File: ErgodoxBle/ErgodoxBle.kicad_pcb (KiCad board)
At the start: 2 copper layers, 181.7 x 158.1 mm, 85 parts, among them K0 KEYSW, K1 KEYSW, K10 KEYSW, K11 KEYSW, K12 KEYSW, K13 KEYSW, K14 KEYSW, K15 KEYSW, K16 KEYSW, K2 KEYSW, K20 KEYSW, K21 KEYSW, K22 KEYSW, K23 KEYSW, K24 KEYSW, K25 KEYSW, K26 KEYSW, K3 KEYSW, K30 KEYSW, K31 KEYSW, K32 KEYSW, K33 KEYSW, K34 KEYSW, K35 KEYSW, K36 KEYSW, K4 KEYSW, K40 KEYSW, K41 KEYSW, K42 KEYSW, K43 KEYSW, K44 KEYSW, K45 KEYSW, K46 KEYSW, K5 KEYSW, K54 KEYSW, K55 KEYSW, K56 KEYSW, K6 KEYSW, SW1 SW_PUSH, SW2 SW_PUSH

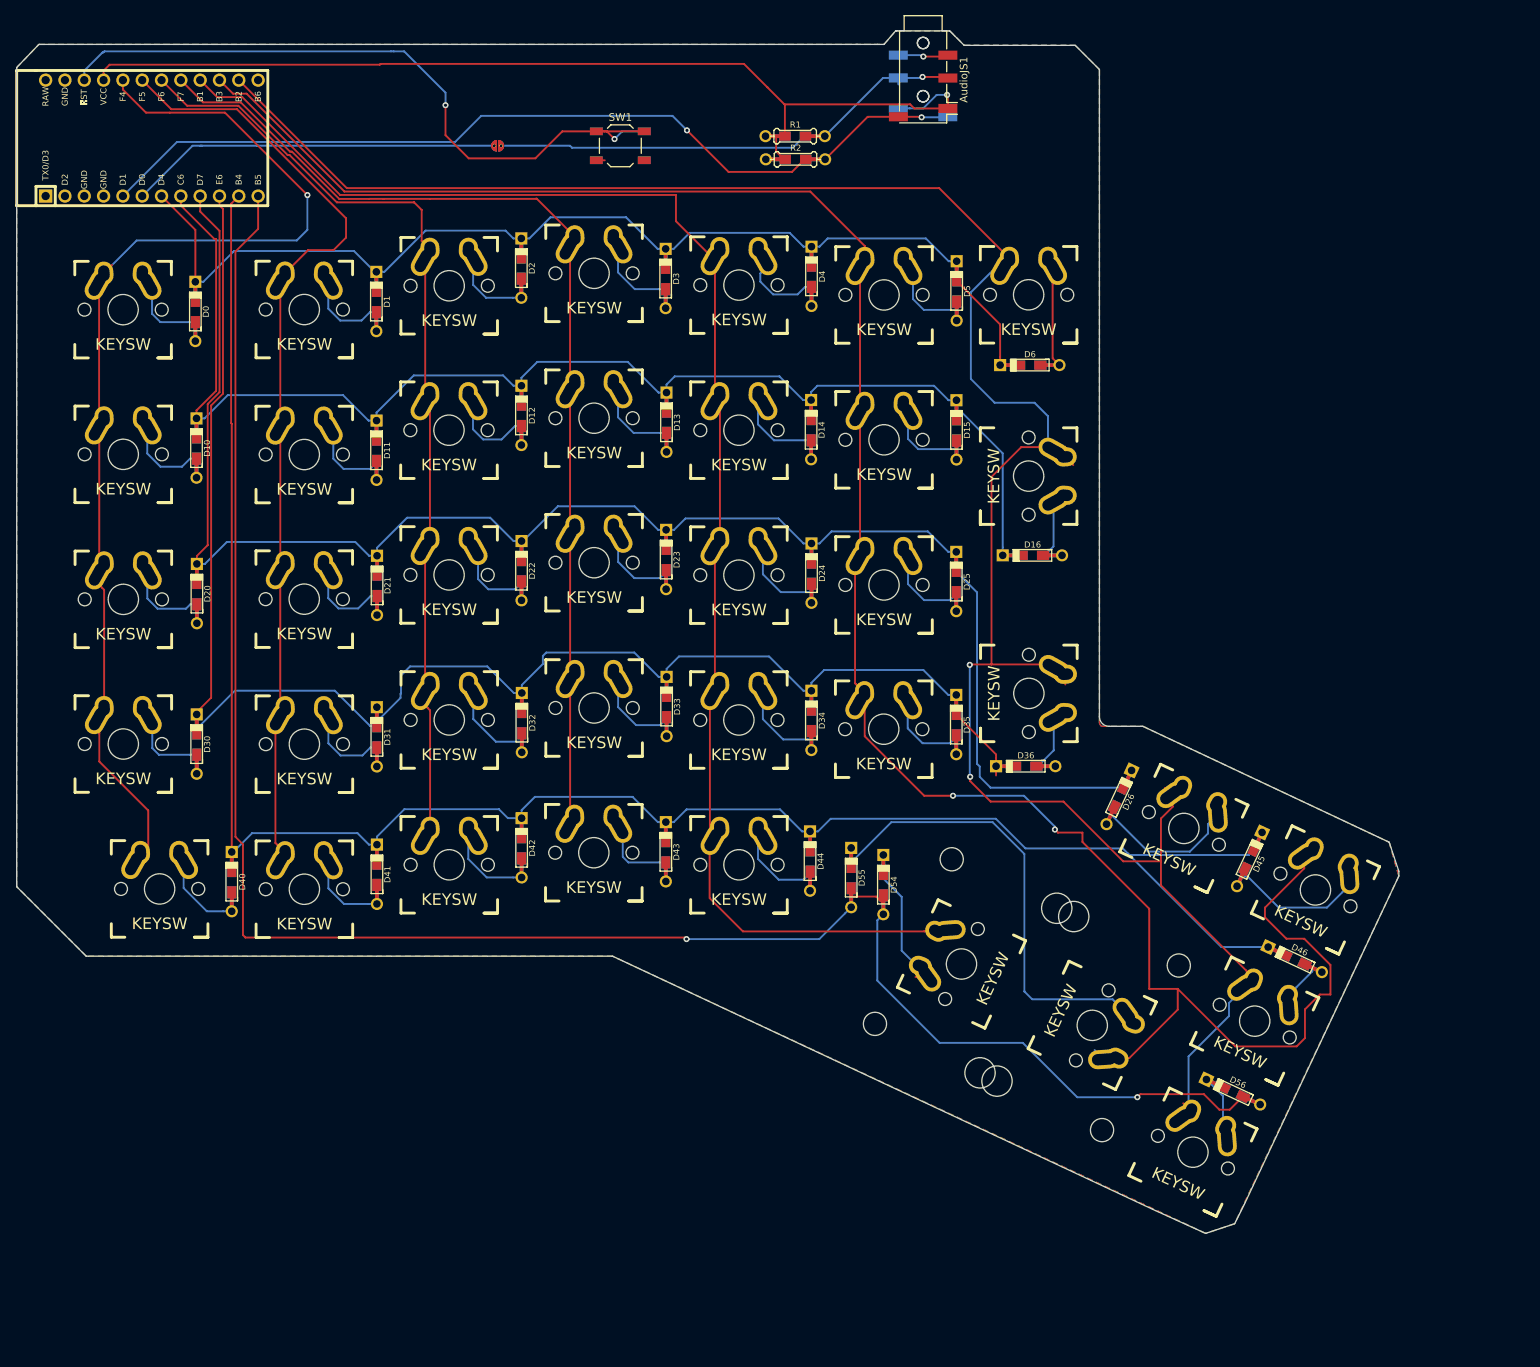
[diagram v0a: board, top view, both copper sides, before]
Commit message: Redo the existing ergodox pcb
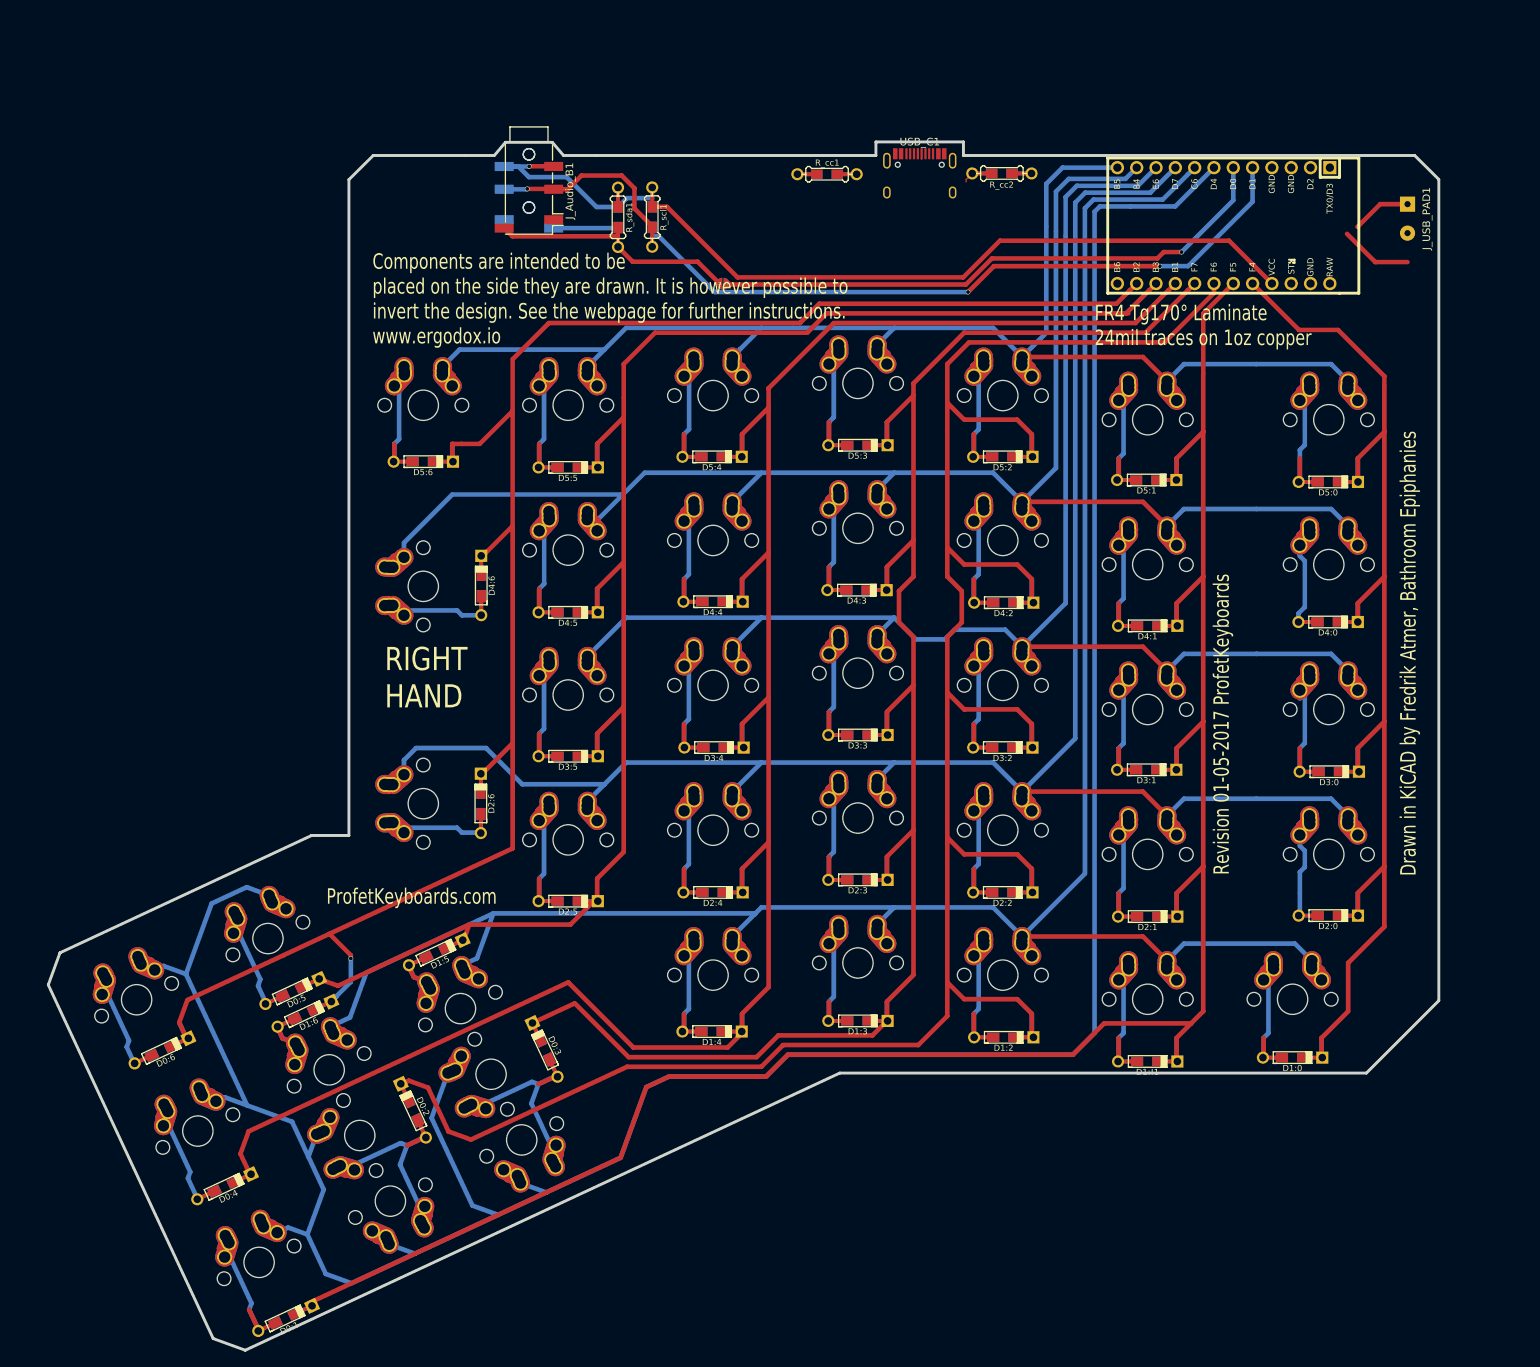
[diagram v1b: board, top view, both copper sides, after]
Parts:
- removed AudioJM1, AudioJS1: AudioJack4, Connector_Audio:Jack_3.5mm_PJ320D_Horizontal
- removed D0, D1, D10, D11, D12, D13, D14, D15, D16, D2, D20, D21, D22, D23, D24, D25, D26, D3, D30, D31, D32, D33, D34, D35, D36, D4, D40, D41, D42, D43, D44, D45, D46, D5, D6: D, Keebio-Parts:Diode-dual
- removed D54, D55, D56: DIODE, Keebio-Parts:Diode-dual
- removed K0, K1, K10, K11, K12, K13, K14, K15, K16, K2, K20, K21, K22, K23, K24, K25, K26, K3, K30, K31, K32, K33, K34, K35, K36, K4, K40, K41, K42, K43, K44, K45, K46, K5, K56, K6: KEYSW, footprints:Mx_Alps_100-dualside
- removed K54, K55: KEYSW, footprints:Mx_Alps_200-dualside
- removed MCU1: ProMicro, Keebio-Parts:ArduinoProMicro
- removed R1, R2: 4.7k, Keebio-Parts:Resistor-Hybrid
- removed SJ1, SJ2: SOLDER_JUMPER, Keebio-Parts:solder_jumper
- removed SW1, SW2: SW_PUSH, Button_Switch_SMD:SW_SPST_TL3342
- added D0:1: D, Keebio-Parts:Diode-dual, F.Cu at (54.2, 185.2)
- added D0:2: D, Keebio-Parts:Diode-dual, F.Cu at (71.1, 157.9)
- added D0:3: D, Keebio-Parts:Diode-dual, F.Cu at (88.4, 149.9)
- added D0:4: D, Keebio-Parts:Diode-dual, F.Cu at (46.2, 167.9)
- added D0:5: D, Keebio-Parts:Diode-dual, F.Cu at (55.2, 142.2)
- added D0:6: D, Keebio-Parts:Diode-dual, F.Cu at (38.0, 150.0)
- added D1:!1: D, Keebio-Parts:Diode-dual, F.Cu at (167.6, 151.4)
- added D1:0: D, Keebio-Parts:Diode-dual, F.Cu at (186.7, 150.9)
- added D1:2: D, Keebio-Parts:Diode-dual, F.Cu at (148.7, 148.2)
- added D1:3: D, Keebio-Parts:Diode-dual, F.Cu at (129.5, 146.1)
- added D1:4: D, Keebio-Parts:Diode-dual, F.Cu at (110.4, 147.4)
- added D1:5: D, Keebio-Parts:Diode-dual, F.Cu at (74.0, 137.1)
- added D1:6: D, Keebio-Parts:Diode-dual, F.Cu at (56.8, 145.2)
- added D2:0: D, Keebio-Parts:Diode-dual, F.Cu at (191.4, 132.2)
- added D2:1: D, Keebio-Parts:Diode-dual, F.Cu at (167.6, 132.3)
- added D2:2: D, Keebio-Parts:Diode-dual, F.Cu at (148.6, 129.2)
- added D2:3: D, Keebio-Parts:Diode-dual, F.Cu at (129.5, 127.5)
- added D2:4: D, Keebio-Parts:Diode-dual, F.Cu at (110.5, 129.2)
- added D2:5: D, Keebio-Parts:Diode-dual, F.Cu at (91.4, 130.3)
- added D2:6: D, Keebio-Parts:Diode-dual, F.Cu at (80.0, 117.4)
- added D3:0: D, Keebio-Parts:Diode-dual, F.Cu at (191.5, 113.3)
- added D3:1: D, Keebio-Parts:Diode-dual, F.Cu at (167.5, 113.0)
- added D3:2: D, Keebio-Parts:Diode-dual, F.Cu at (148.6, 110.1)
- added D3:3: D, Keebio-Parts:Diode-dual, F.Cu at (129.5, 108.5)
- added D3:4: D, Keebio-Parts:Diode-dual, F.Cu at (110.6, 110.1)
- added D3:5: D, Keebio-Parts:Diode-dual, F.Cu at (91.4, 111.3)
- added D4:0: D, Keebio-Parts:Diode-dual, F.Cu at (191.4, 93.6)
- added D4:1: D, Keebio-Parts:Diode-dual, F.Cu at (167.6, 94.1)
- added D4:2: D, Keebio-Parts:Diode-dual, F.Cu at (148.7, 91.1)
- added D4:3: D, Keebio-Parts:Diode-dual, F.Cu at (129.4, 89.4)
- added D4:4: D, Keebio-Parts:Diode-dual, F.Cu at (110.5, 90.9)
- added D4:5: D, Keebio-Parts:Diode-dual, F.Cu at (91.4, 92.3)
- added D4:6: D, Keebio-Parts:Diode-dual, F.Cu at (80.0, 88.8)
- added D5:0: D, Keebio-Parts:Diode-dual, F.Cu at (191.4, 75.2)
- added D5:1: D, Keebio-Parts:Diode-dual, F.Cu at (167.5, 74.9)
- added D5:2: D, Keebio-Parts:Diode-dual, F.Cu at (148.6, 71.9)
- added D5:3: D, Keebio-Parts:Diode-dual, F.Cu at (129.5, 70.4)
- added D5:4: D, Keebio-Parts:Diode-dual, F.Cu at (110.4, 71.9)
- added D5:5: D, Keebio-Parts:Diode-dual, F.Cu at (91.4, 73.3)
- added D5:6: D, Keebio-Parts:Diode-dual, F.Cu at (72.4, 72.5)
- added JP1: SolderJumper_2_Open, Keebio-Parts:solder_jumper, F.Cu at (111.8, 49.1)
- added J_Audio_B1: AudioJack4, Connector_Audio:Jack_3.5mm_PJ320D_Horizontal, F.Cu at (86.3, 36.9)
- added J_Audio_F1: AudioJack4, Connector_Audio:Jack_3.5mm_PJ320D_Horizontal, B.Cu at (86.3, 36.9)
- added J_USB_PAD1: Conn_01x02_Female, Connector_Wire:SolderWirePad_1x02_P3.81mm_Drill0.8mm, F.Cu at (201.8, 38.7)
- added R_cc1: 5.1K, Keebio-Parts:Resistor-Hybrid, F.Cu at (125.5, 34.7)
- added R_cc2: 5.1K, Keebio-Parts:Resistor-Hybrid, F.Cu at (148.5, 34.6)
- added R_scl1: 47k, Keebio-Parts:Resistor-Hybrid, F.Cu at (102.5, 40.4)
- added R_sda1: 47k, Keebio-Parts:Resistor-Hybrid, F.Cu at (98.0, 40.4)
- added SW0:10: SW0:3, Keebio-Parts:Hybrid_PCB_100H_Dual_hole, F.Cu at (81.3, 153.1)
- added SW0:11: SW0:2, Keebio-Parts:Hybrid_PCB_100H_Dual_hole, F.Cu at (64.0, 161.1)
- added SW0:12: SW0:1, Keebio-Parts:Hybrid_PCB_100H_Dual_hole, F.Cu at (50.8, 177.8)
- added SW0:7: SW0:6, Keebio-Parts:Hybrid_PCB_100H_Dual_hole, F.Cu at (34.7, 143.3)
- added SW0:8: SW0:5, Keebio-Parts:Hybrid_PCB_100H_Dual_hole, F.Cu at (52.0, 135.2)
- added SW0:9: SW0:4, Keebio-Parts:Hybrid_PCB_100H_Dual_hole, F.Cu at (42.7, 160.5)
- added SW1:10: SW1:3, Keebio-Parts:Hybrid_PCB_100H_Dual_hole, F.Cu at (129.5, 138.4)
- added SW1:11: SW1:2, Keebio-Parts:Hybrid_PCB_100H_Dual_hole, F.Cu at (148.6, 140.0)
- added SW1:12: SW1:1, Keebio-Parts:Hybrid_PCB_100H_Dual_hole, F.Cu at (167.6, 143.2)
- added SW1:13: SW1:0, Keebio-Parts:Hybrid_PCB_100H_Dual_hole, F.Cu at (186.7, 143.2)
- added SW1:9: SW1:4, Keebio-Parts:Hybrid_PCB_100H_Dual_hole, F.Cu at (110.5, 140.0)
- added SW2:10: SW2:3, Keebio-Parts:Hybrid_PCB_100H_Dual_hole, F.Cu at (129.5, 119.4)
- added SW2:11: SW2:2, Keebio-Parts:Hybrid_PCB_100H_Dual_hole, F.Cu at (148.6, 121.0)
- added SW2:12: SW2:1, Keebio-Parts:Hybrid_PCB_100H_Dual_hole, F.Cu at (167.6, 124.2)
- added SW2:13: SW2:0, Keebio-Parts:Hybrid_PCB_100H_Dual_hole, F.Cu at (191.5, 124.2)
- added SW2:7: SW2:6, Keebio-Parts:Hybrid_PCB_100H_Dual_hole, F.Cu at (72.4, 117.5)
- added SW2:8: SW2:5, Keebio-Parts:Hybrid_PCB_100H_Dual_hole, F.Cu at (91.4, 122.2)
- added SW2:9: SW2:4, Keebio-Parts:Hybrid_PCB_100H_Dual_hole, F.Cu at (110.5, 121.0)
- added SW3:10: SW3:3, Keebio-Parts:Hybrid_PCB_100H_Dual_hole, F.Cu at (129.5, 100.3)
- added SW3:11: SW3:2, Keebio-Parts:Hybrid_PCB_100H_Dual_hole, F.Cu at (148.6, 101.9)
- added SW3:12: SW3:1, Keebio-Parts:Hybrid_PCB_100H_Dual_hole, F.Cu at (167.6, 105.1)
- added SW3:13: SW3:0, Keebio-Parts:Hybrid_PCB_100H_Dual_hole, F.Cu at (191.5, 105.1)
- added SW3:8: SW3:5, Keebio-Parts:Hybrid_PCB_100H_Dual_hole, F.Cu at (91.4, 103.2)
- added SW3:9: SW3:4, Keebio-Parts:Hybrid_PCB_100H_Dual_hole, F.Cu at (110.5, 101.9)
- added SW4:10: SW4:3, Keebio-Parts:Hybrid_PCB_100H_Dual_hole, F.Cu at (129.5, 81.3)
- added SW4:11: SW4:2, Keebio-Parts:Hybrid_PCB_100H_Dual_hole, F.Cu at (148.6, 82.9)
- added SW4:12: SW4:1, Keebio-Parts:Hybrid_PCB_100H_Dual_hole, F.Cu at (167.6, 86.1)
- added SW4:13: SW4:0, Keebio-Parts:Hybrid_PCB_100H_Dual_hole, F.Cu at (191.5, 86.1)
- added SW4:7: SW4:6, Keebio-Parts:Hybrid_PCB_100H_Dual_hole, F.Cu at (72.4, 88.9)
- added SW4:8: SW4:5, Keebio-Parts:Hybrid_PCB_100H_Dual_hole, F.Cu at (91.4, 84.1)
- added SW4:9: SW4:4, Keebio-Parts:Hybrid_PCB_100H_Dual_hole, F.Cu at (110.5, 82.9)
- added SW5:10: SW5:3, Keebio-Parts:Hybrid_PCB_100H_Dual_hole, F.Cu at (129.5, 62.2)
- added SW5:11: SW5:2, Keebio-Parts:Hybrid_PCB_100H_Dual_hole, F.Cu at (148.6, 63.8)
- added SW5:12: SW5:1, Keebio-Parts:Hybrid_PCB_100H_Dual_hole, F.Cu at (167.6, 67.0)
- added SW5:13: SW5:0, Keebio-Parts:Hybrid_PCB_100H_Dual_hole, F.Cu at (191.5, 67.0)
- added SW5:7: SW5:6, Keebio-Parts:Hybrid_PCB_100H_Dual_hole, F.Cu at (72.4, 65.1)
- added SW5:8: SW5:5, Keebio-Parts:Hybrid_PCB_100H_Dual_hole, F.Cu at (91.4, 65.1)
- added SW5:9: SW5:4, Keebio-Parts:Hybrid_PCB_100H_Dual_hole, F.Cu at (110.5, 63.8)
- added SX0:10: SX0:3, Keebio-Parts:Hybrid_PCB_100H_Dual_hole, F.Cu at (85.3, 161.7)
- added SX0:11: SX0:2, Keebio-Parts:Hybrid_PCB_100H_Dual_hole, F.Cu at (68.1, 169.7)
- added SX1:7: SX1:6, Keebio-Parts:Hybrid_PCB_100H_Dual_hole, F.Cu at (60.0, 152.5)
- added SX1:8: SX1:5, Keebio-Parts:Hybrid_PCB_100H_Dual_hole, F.Cu at (77.3, 144.4)
- added USB_C1: HRO-TYPE-C-31-M-12, usbc_footprint:HRO-TYPE-C-31-M-12, F.Cu at (137.7, 39.7)
- added proMicro1: ProMicro, Keebio-Parts:ArduinoProMicro, F.Cu at (177.6, 41.5)
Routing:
- net /ROW0: track 0.00 -> 400.6 mm
- net /ROW1: track 0.00 -> 314.9 mm
- net /COL11: track 0.00 -> 298.0 mm
- net COL6: track 295.5 -> 0.00 mm, vias 2 -> 0
- net /ROW2: track 0.00 -> 284.6 mm
- net COL5: track 283.8 -> 0.00 mm, vias 2 -> 0
- net /COL1: track 0.00 -> 277.3 mm
- net /COL4: track 0.00 -> 267.3 mm
- net ROW4: track 258.6 -> 0.00 mm
- net ROW5: track 250.6 -> 0.00 mm, vias 2 -> 0
- net /ROW4: track 0.00 -> 246.3 mm
- net /COL6: track 0.00 -> 244.2 mm, vias 0 -> 1
- net /ROW3: track 0.00 -> 228.3 mm
- net /COL10: track 0.00 -> 224.1 mm
- net /COL5: track 0.00 -> 219.1 mm
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- removed copper zone on B.Cu, net GND
- removed copper zone on F.Cu, net GND
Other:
- board size 181.7 x 158.1 mm -> 182.8 x 158.9 mm
- net class Default: clearance 0.2 -> 0.3048; trace_width 0.25 -> 0.6; via_dia 0.8 -> 0.6096; via_drill 0.4 -> 0.508
- rule pad_to_mask_clearance: 0.051 -> 0.2032
- rule trace_clearance: 0.2 -> 0.3048
- rule trace_min: 0.2 -> 0.0254
- rule via_min_drill: 0.3 -> 0.2032
- rule via_min_size: 0.4 -> 0.4064
- board text added: "Components are intended to be placed on the side they are drawn. It is however possible to invert the design. See the webpage for further instructions. www.ergodox.io"
- board text added: "Design by Dominic Beauchamp, based on the Key64 by Nestor A. Diaz"
- board text added: "Drawn in KiCAD by Fredrik Atmer, Bathroom Epiphanies"
- board text added: "ErgoDox"
- board text added: "FR4 Tg170° Laminate 24mil traces on 1oz copper"
- board text added: "LEFT HAND"
- board text added: "ProfetKeyboards.com"
- board text added: "RIGHT HAND"
- board text added: "Revision 01-05-2017 ProfetKeyboards"

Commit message: Added USB-C
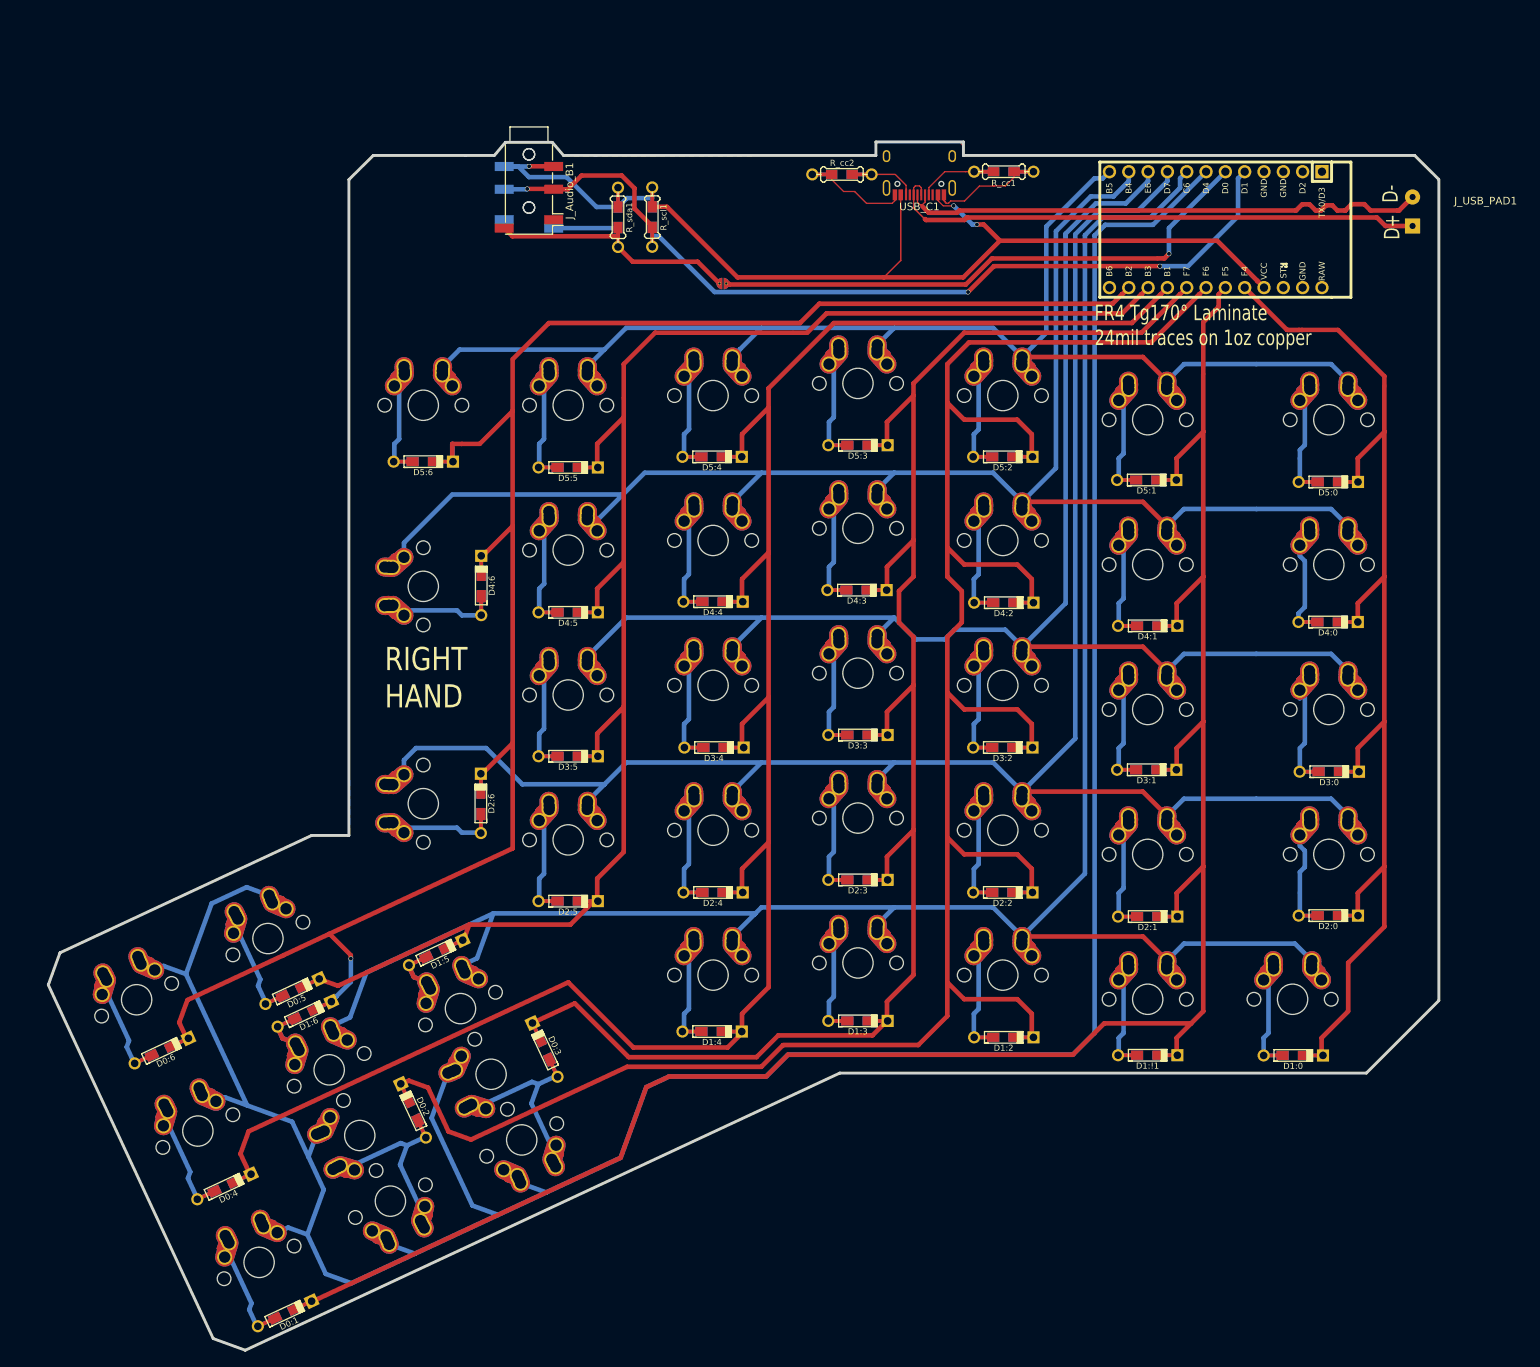
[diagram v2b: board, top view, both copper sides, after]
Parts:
- moved R_cc1 23.2 mm to (148.7, 34.4), turned to 0 degrees
- moved R_cc2 21.0 mm to (127.4, 34.7), turned to 180 degrees
- moved USB_C1 9.98 mm to (137.6, 29.7), turned to 180 degrees
- moved J_USB_PAD1 2.95 mm to (202.5, 41.5), turned to 90 degrees
- moved proMicro1 1.17 mm to (176.6, 42.0)
- moved D1:!1 0.82 mm to (167.6, 150.6)
- moved D0:1 0.62 mm to (54.2, 184.5)
- moved D1:0 0.30 mm to (186.8, 150.6)
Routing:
- net /D+: track 7.84 -> 71.7 mm
- net /D-: track 9.51 -> 71.0 mm
- net GND: track 0.00 -> 23.5 mm
- net /Vcc: track 118.3 -> 140.4 mm, vias 1 -> 3
- net /COL11: track 298.0 -> 283.3 mm
- net /COL4: track 267.3 -> 253.3 mm
- net /COL10: track 224.1 -> 210.1 mm
- net /COL1: track 277.3 -> 263.6 mm
- net /COL0: track 157.9 -> 146.1 mm
- net /COL5: track 219.1 -> 209.9 mm
- net /CC1: track 0.00 -> 7.77 mm
- net /CC2: track 1.46 -> 6.39 mm
- net /ROW5: track 211.3 -> 206.7 mm
- net /COL6: track 244.2 -> 240.4 mm
- net /ROW4: track 246.3 -> 242.7 mm
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- added copper zone on B.Cu, net GND
- added copper zone on F.Cu, net GND
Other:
- board text added: "D+"
- board text added: "D-"
- board text removed: "Components are intended to be placed on the side they are drawn. It is however possible to invert the design. See the webpage for further instructions. www.ergodox.io"
- board text removed: "Design by Dominic Beauchamp, based on the Key64 by Nestor A. Diaz"
- board text removed: "Drawn in KiCAD by Fredrik Atmer, Bathroom Epiphanies"
- board text removed: "ErgoDox"
- board text removed: "ProfetKeyboards.com"
- board text removed: "Revision 01-05-2017 ProfetKeyboards"

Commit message: finalize pcb
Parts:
- added REF**: via-0.6mm, usbc_footprint:via-0.6mm, F.Cu at (172.9, 56.5)
- added REF**: via-0.6mm, usbc_footprint:via-0.6mm, F.Cu at (143.3, 76.1)
- added REF**: via-0.6mm, usbc_footprint:via-0.6mm, F.Cu at (67.8, 145.7)
- added REF**: via-0.6mm, usbc_footprint:via-0.6mm, F.Cu at (96.1, 157.6)
- added REF**: via-0.6mm, usbc_footprint:via-0.6mm, F.Cu at (158.3, 141.6)
- added REF**: via-0.6mm, usbc_footprint:via-0.6mm, F.Cu at (149.2, 145.2)
- added REF**: via-0.6mm, usbc_footprint:via-0.6mm, F.Cu at (142.6, 147.3)
- added REF**: via-0.6mm, usbc_footprint:via-0.6mm, F.Cu at (156.2, 126.8)
- added REF**: via-0.6mm, usbc_footprint:via-0.6mm, F.Cu at (154.9, 87.9)
- added REF**: via-0.6mm, usbc_footprint:via-0.6mm, F.Cu at (156.0, 105.3)
- added REF**: via-0.6mm, usbc_footprint:via-0.6mm, F.Cu at (156.3, 113.7)
- added REF**: via-0.6mm, usbc_footprint:via-0.6mm, F.Cu at (60.6, 176.1)
- added REF**: via-0.6mm, usbc_footprint:via-0.6mm, F.Cu at (91.8, 70.0)
- added REF**: via-0.6mm, usbc_footprint:via-0.6mm, F.Cu at (167.9, 110.0)
- added REF**: via-0.6mm, usbc_footprint:via-0.6mm, F.Cu at (138.9, 141.5)
- added REF**: via-0.6mm, usbc_footprint:via-0.6mm, F.Cu at (121.4, 84.8)
- added REF**: via-0.6mm, usbc_footprint:via-0.6mm, F.Cu at (121.4, 67.6)
- added REF**: via-0.6mm, usbc_footprint:via-0.6mm, F.Cu at (120.7, 124.0)
- added REF**: via-0.6mm, usbc_footprint:via-0.6mm, F.Cu at (123.4, 104.2)
- added REF**: via-0.6mm, usbc_footprint:via-0.6mm, F.Cu at (92.4, 88.5)
- added REF**: via-0.6mm, usbc_footprint:via-0.6mm, F.Cu at (103.5, 76.0)
- added REF**: via-0.6mm, usbc_footprint:via-0.6mm, F.Cu at (73.4, 164.6)
- added REF**: via-0.6mm, usbc_footprint:via-0.6mm, F.Cu at (177.3, 37.8)
- added REF**: via-0.6mm, usbc_footprint:via-0.6mm, F.Cu at (91.8, 108.3)
- added REF**: via-0.6mm, usbc_footprint:via-0.6mm, F.Cu at (168.9, 71.3)
- added REF**: via-0.6mm, usbc_footprint:via-0.6mm, F.Cu at (149.0, 49.6)
- added REF**: via-0.6mm, usbc_footprint:via-0.6mm, F.Cu at (139.6, 45.1)
- added REF**: via-0.6mm, usbc_footprint:via-0.6mm, F.Cu at (148.9, 68.7)
